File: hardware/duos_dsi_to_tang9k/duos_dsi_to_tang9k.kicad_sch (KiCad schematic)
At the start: 6 parts, among them J1 CON26A_Duo_S, J2 Tang_Nano_9K

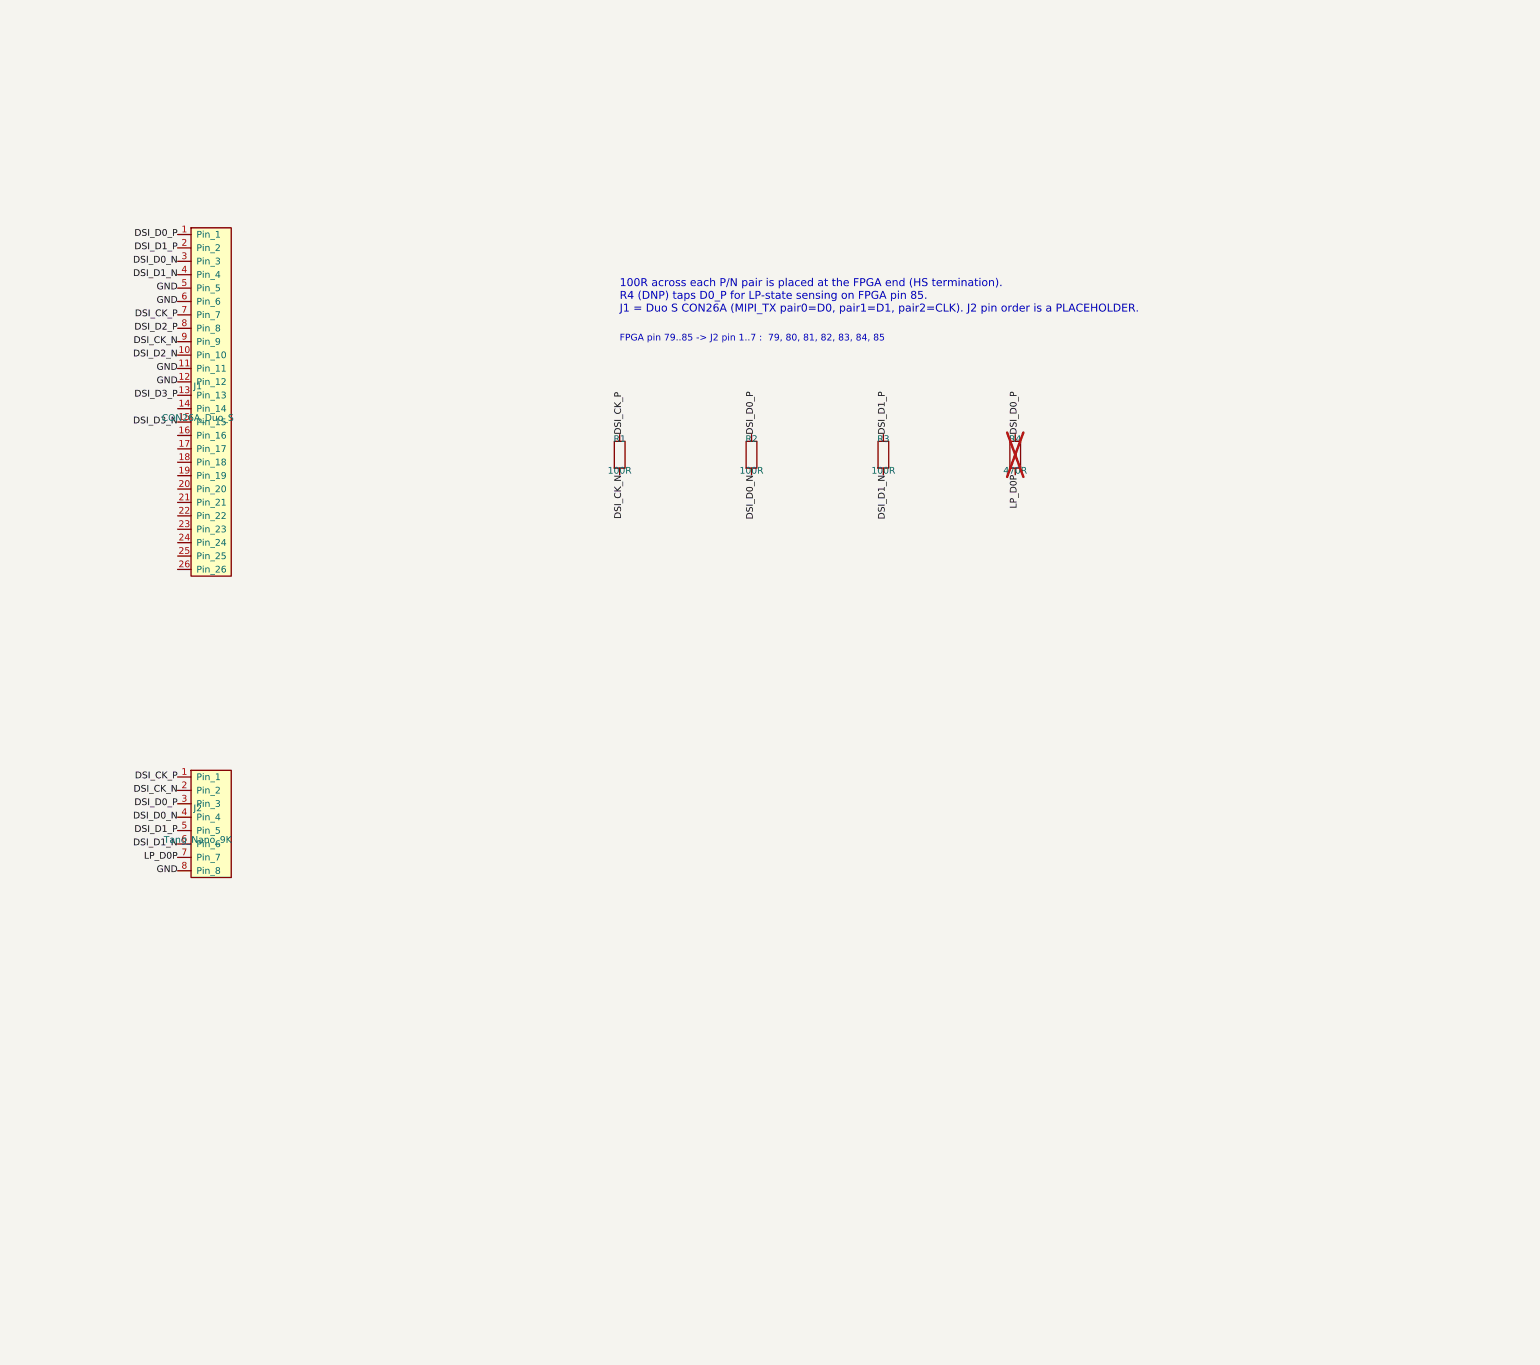
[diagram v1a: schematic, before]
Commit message: DSI adapter: Tang header pinout, split termination, LP level shifters on pins 25/26
Co-Authored-By: Claude Sonnet 5.5 <noreply@anthropic.com>
Claude-Session: https://claude.ai/code/session_01Kmp7iiQhgLgwfNawdP6KaV
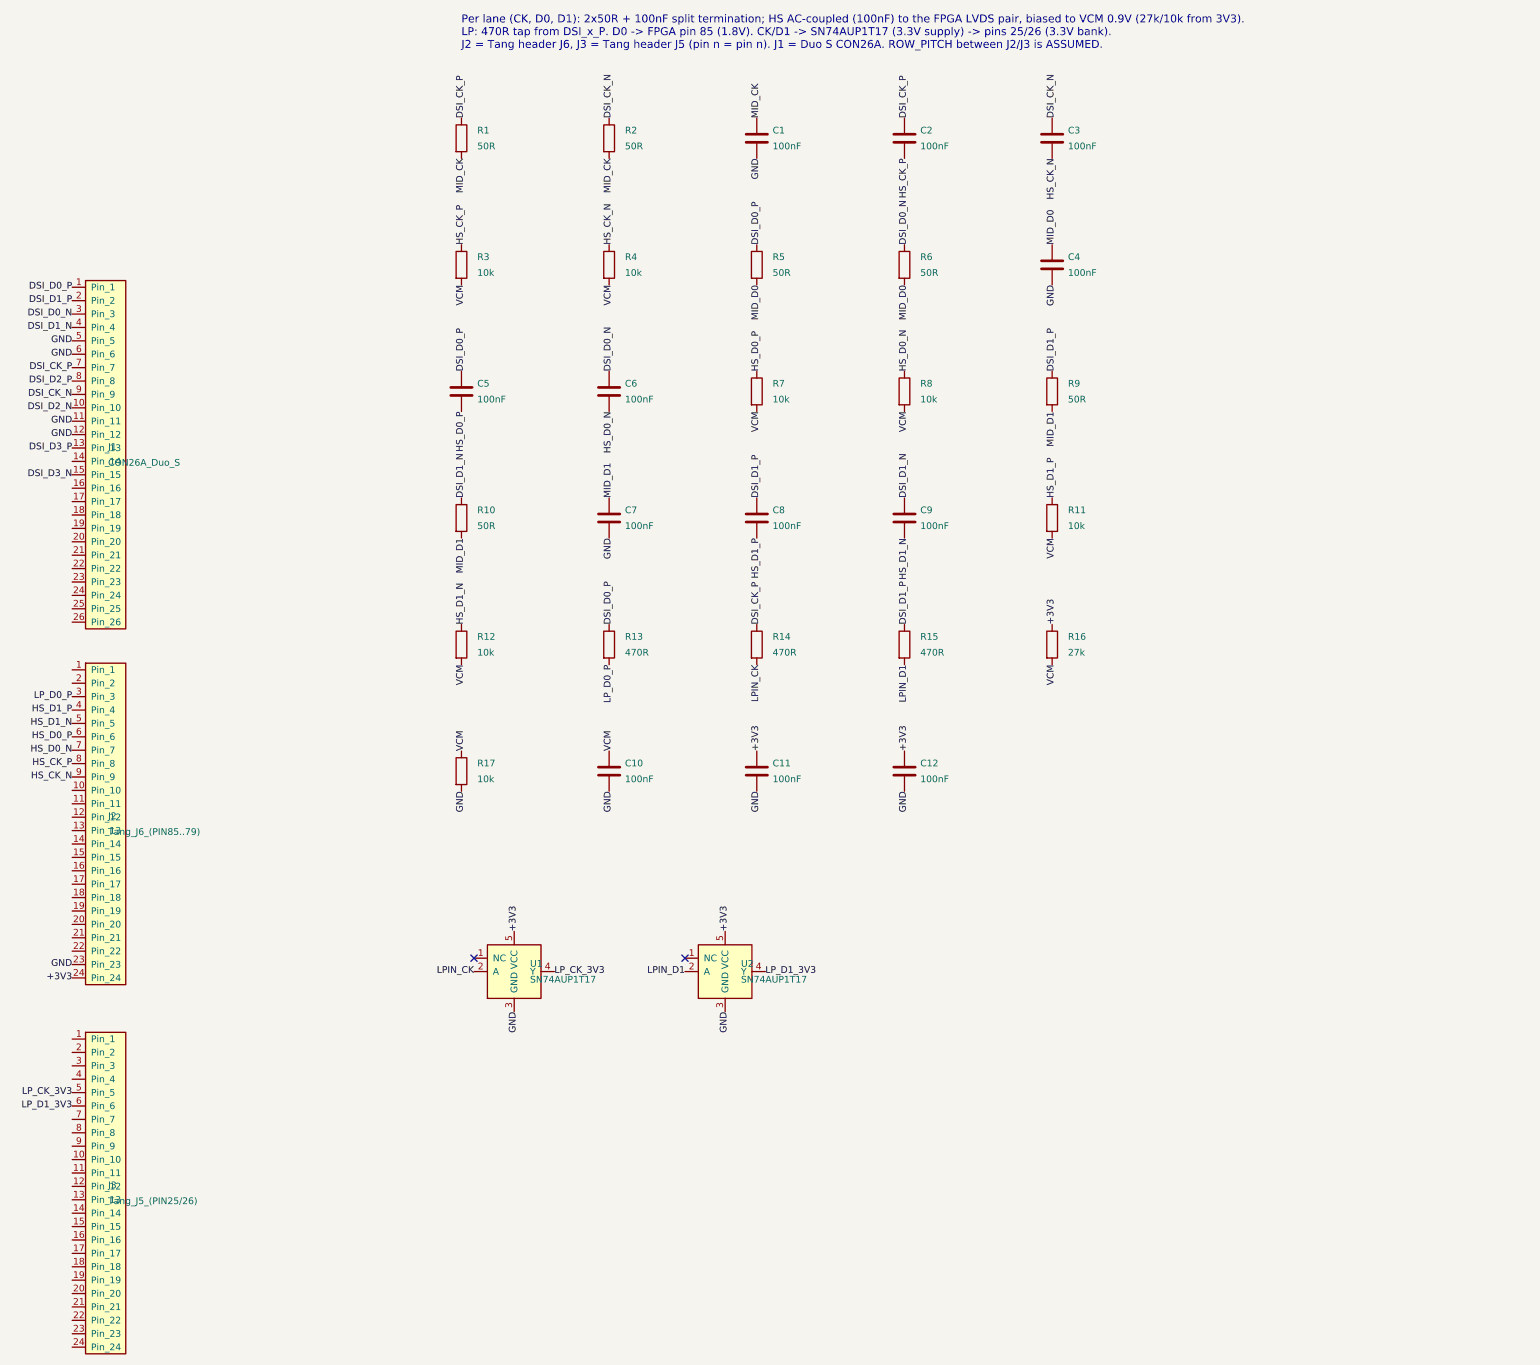
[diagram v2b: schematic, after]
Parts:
- removed J2: Tang_Nano_9K, Connector_PinHeader_2.54mm:PinHeader_1x08_P2.54mm_Vertical, symbol Connector_Generic:Conn_01x08
- added C1, C10, C11, C12, C2, C3, C4, C5, C6, C7, C8, C9: 100nF, Capacitor_SMD:C_0402_1005Metric, symbol Device:C
- added J2: Tang_J6_(PIN85..79), Connector_PinHeader_2.54mm:PinHeader_1x24_P2.54mm_Vertical, symbol Connector_Generic:Conn_01x24
- added J3: Tang_J5_(PIN25/26), Connector_PinHeader_2.54mm:PinHeader_1x24_P2.54mm_Vertical, symbol Connector_Generic:Conn_01x24
- added R10, R5, R6, R9: 50R, Resistor_SMD:R_0402_1005Metric, symbol Device:R
- added R11, R12, R17, R7, R8: 10k, Resistor_SMD:R_0402_1005Metric, symbol Device:R
- added R13, R14, R15: 470R, Resistor_SMD:R_0402_1005Metric, symbol Device:R
- added R16: 27k, Resistor_SMD:R_0402_1005Metric, symbol Device:R
- added U1, U2: SN74AUP1T17, Package_TO_SOT_SMD:SOT-23-5, symbol Custom:SN74AUP1T17
- R1, R2: value 100R -> 50R
- R3: value 100R -> 10k
- R4: value 470R -> 10k; now fitted
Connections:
- net DSI_CK_N: now also R2.1, C3.1; no longer R1.2
- net DSI_CK_P: now also C2.1, R14.1
- net DSI_D0_N: now also C6.1, R6.1; no longer R2.2
- net DSI_D0_P: now also C5.1, R13.1, R5.1; no longer R2.1, R4.1
- net DSI_D1_N: now also C9.1, R10.1; no longer R3.2
- net DSI_D1_P: now also C8.1, R15.1, R9.1; no longer R3.1
- net GND: now also C1.2, C10.2, C11.2, C12.2, C4.2, C7.2, J2.23 (Pin_23), R17.2, U1.3 (GND), U2.3 (GND)
- net LP_D0P renamed VCM
- net VCM: now also R3.2, C10.1, R11.2, R12.2, R16.2, R17.1, R7.2, R8.2
- new net +3V3: C11.1, C12.1, J2.24 (Pin_24), R16.1, U1.5 (VCC), U2.5 (VCC)
- new net HS_CK_N: C3.2, J2.9 (Pin_9), R4.1
- new net HS_CK_P: C2.2, J2.8 (Pin_8), R3.1
- new net HS_D0_N: C6.2, J2.7 (Pin_7), R8.1
- new net HS_D0_P: C5.2, J2.6 (Pin_6), R7.1
- new net HS_D1_N: C9.2, J2.5 (Pin_5), R12.1
- new net HS_D1_P: C8.2, J2.4 (Pin_4), R11.1
- new net LPIN_CK: R14.2, U1.2 (A)
- new net LPIN_D1: R15.2, U2.2 (A)
- new net LP_CK_3V3: J3.5 (Pin_5), U1.4 (Y)
- new net LP_D0_P: J2.3 (Pin_3), R13.2
- new net LP_D1_3V3: J3.6 (Pin_6), U2.4 (Y)
- new net MID_CK: C1.1, R1.2, R2.2
- new net MID_D0: C4.1, R5.2, R6.2
- new net MID_D1: C7.1, R10.2, R9.2
- no-connect marks 0 -> 2
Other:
- note added: "Per lane (CK, D0, D1): 2x50R + 100nF split termination; HS AC-coupled (100nF) to the FPGA LVDS pair, biased to VCM 0.9V (27k/10k from 3V3). LP: 470R tap from DSI_x_P. D0 -> FPGA pin 85 (1.8V). CK/D1 -> SN74AUP1T17 (3.3V supply) -> pins 25/26 (3.3V bank). J2 = Tang header J6, J3 = Tang header J5 (pin n = pin n). J1 = Duo S CON26A. ROW_PITCH between J2/J3 is ASSUMED."
- note removed: "100R across each P/N pair is placed at the FPGA end (HS termination). R4 (DNP) taps D0_P for LP-state sensing on FPGA pin 85. J1 = Duo S CON26A (MIPI_TX pair0=D0, pair1=D1, pair2=CLK). J2 pin order is a PLACEHOLDER."
- note removed: "FPGA pin 79..85 -> J2 pin 1..7 : 79, 80, 81, 82, 83, 84, 85"
